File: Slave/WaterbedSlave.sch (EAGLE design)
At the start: 10 parts

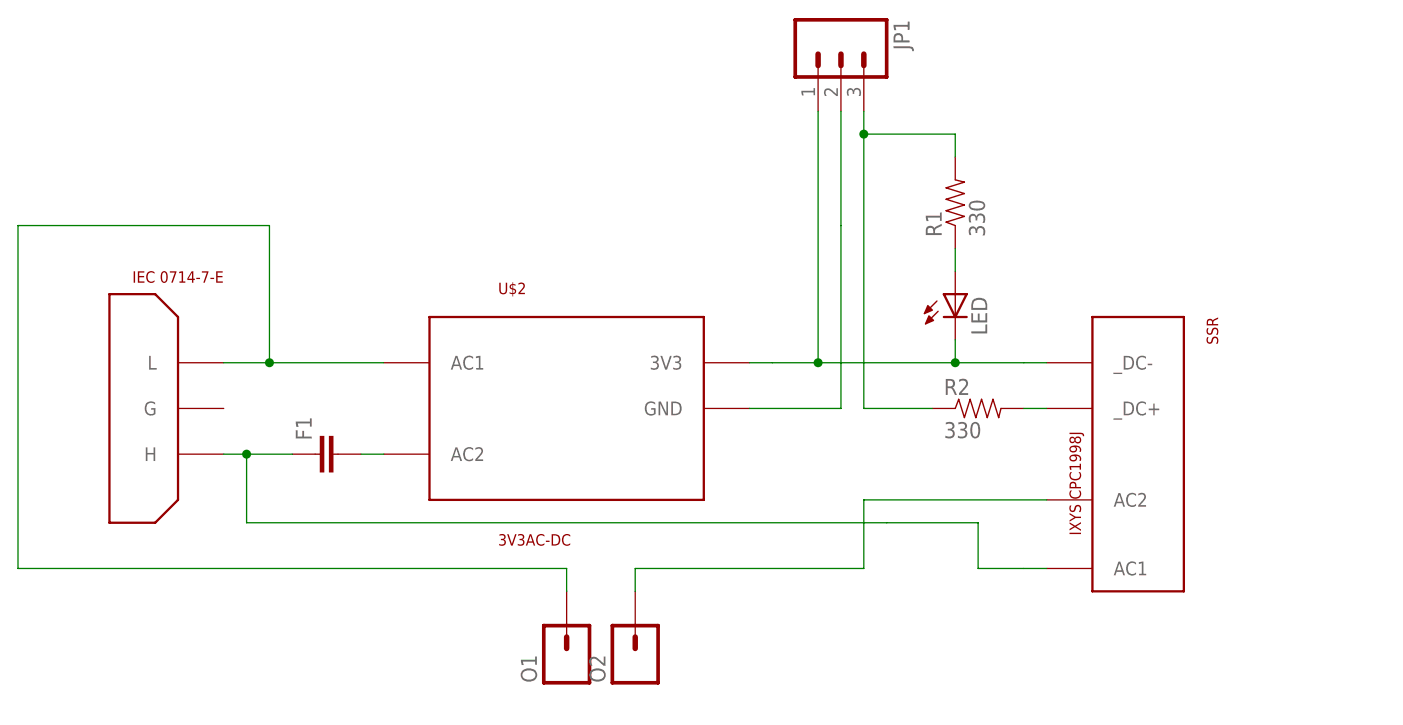
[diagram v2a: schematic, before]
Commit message: The cheap AC-DC sucked. Using trusted brand.
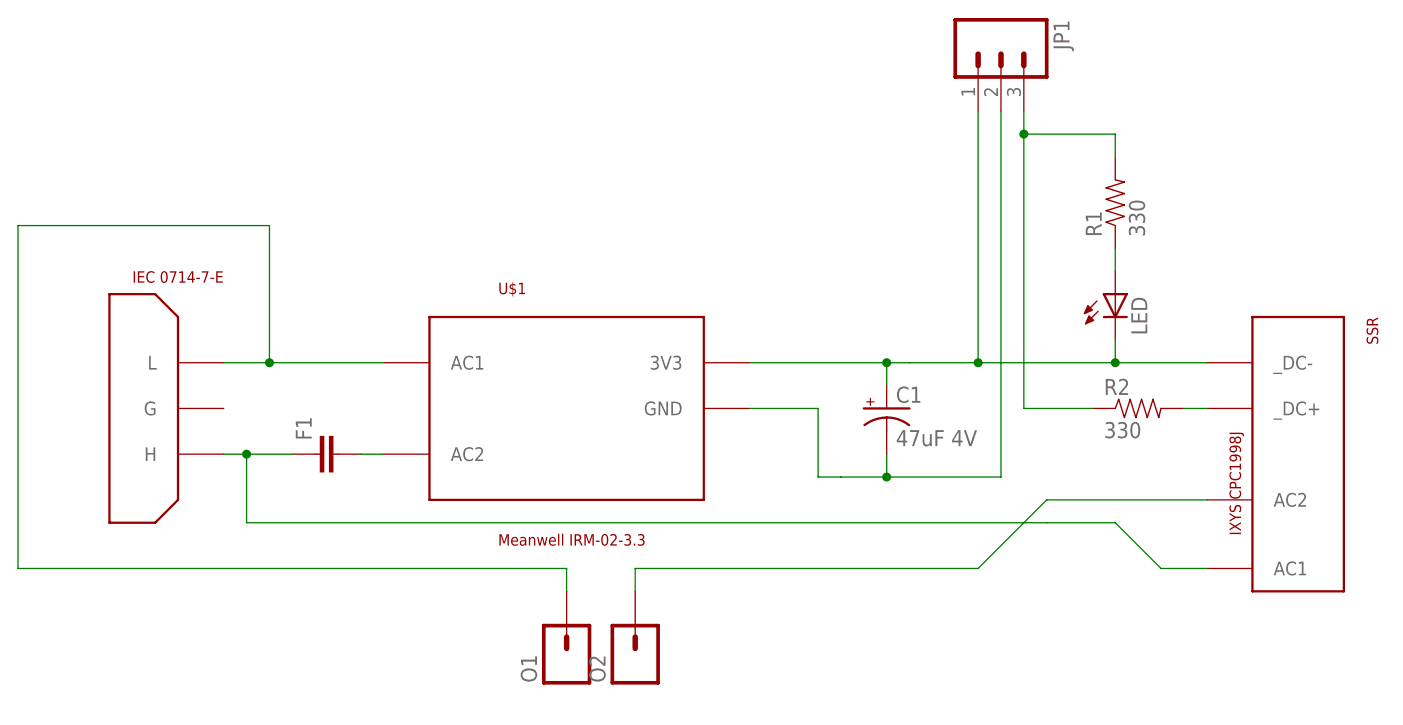
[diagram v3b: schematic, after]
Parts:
- removed U$2: 3V3AC-DC, CuriousTech:RAC02-3.3SCCHEAP
- added C1: 47uF 4V, SparkFun-Capacitors:CAP_POLPTH2
- added U$1: Meanwell IRM-02-3.3, CuriousTech:RAC02-3.3SC
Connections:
- net GND: now also C1.+, U$1.3V3; no longer U$2.3V3
- net N$1: now also U$1.AC1; no longer U$2.AC1
- net N$15: now also C1.-, U$1.GND; no longer U$2.GND
- net N$2: now also U$1.AC2; no longer U$2.AC2
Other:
- moved on the sheet: JP1, LED, R1, R2, SSR
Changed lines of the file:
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@@
 <part name="R1" library="SparkFun-Resistors" deviceset="RESISTOR" device="0805-RES" value="330"/>
 <part name="SSR" library="CuriousTech" deviceset="SSR-5A-240VAC" device="I4-PAC" value="IXYS CPC1998J"/>
-<part name="U$2" library="CuriousTech" deviceset="RAC02-3.3SC" device="CHEAP" value="3V3AC-DC"/>
 <part name="R2" library="SparkFun-Resistors" deviceset="RESISTOR" device="0805-RES" value="330"/>
+<part name="U$1" library="CuriousTech" deviceset="RAC02-3.3SC" device="" value="Meanwell IRM-02-3.3"/>
+<part name="C1" library="SparkFun-Capacitors" deviceset="CAP_POL" device="PTH2" value="47uF 4V"/>
 </parts>
 <sheets>
@@
 </plain>
 <instances>
-<instance part="JP1" gate="G$1" x="91.44" y="101.6" rot="R270"/>
+<instance part="JP1" gate="G$1" x="109.22" y="101.6" rot="R270"/>
 <instance part="U$3" gate="G$1" x="17.78" y="55.88" rot="MR180"/>
 <instance part="O1" gate="G$1" x="60.96" y="33.02" rot="R90"/>
 <instance part="O2" gate="G$1" x="68.58" y="33.02" rot="R90"/>
 <instance part="F1" gate="G$1" x="35.56" y="55.88" rot="R90"/>
-<instance part="LED" gate="G$1" x="104.14" y="73.66"/>
-<instance part="R1" gate="G$1" x="104.14" y="83.82" rot="R90"/>
-<instance part="SSR" gate="G$1" x="124.46" y="55.88" rot="R270"/>
-<instance part="U$2" gate="G$1" x="60.96" y="60.96"/>
-<instance part="R2" gate="G$1" x="106.68" y="60.96"/>
+<instance part="LED" gate="G$1" x="121.92" y="73.66"/>
+<instance part="R1" gate="G$1" x="121.92" y="83.82" rot="R90"/>
+<instance part="SSR" gate="G$1" x="142.24" y="55.88" rot="R270"/>
+<instance part="R2" gate="G$1" x="124.46" y="60.96"/>
+<instance part="U$1" gate="G$1" x="60.96" y="60.96"/>
+<instance part="C1" gate="G$1" x="96.52" y="60.96"/>
 </instances>
 <busses>
@@
 <segment>
 <pinref part="JP1" gate="G$1" pin="1"/>
-<wire x1="88.9" y1="66.04" x2="88.9" y2="93.98" width="0.1524" layer="91"/>
-<junction x="88.9" y="66.04"/>
-<wire x1="104.14" y1="66.04" x2="88.9" y2="66.04" width="0.1524" layer="91"/>
-<wire x1="81.28" y1="66.04" x2="83.82" y2="66.04" width="0.1524" layer="91"/>
-<wire x1="83.82" y1="66.04" x2="88.9" y2="66.04" width="0.1524" layer="91"/>
+<wire x1="106.68" y1="66.04" x2="106.68" y2="93.98" width="0.1524" layer="91"/>
+<junction x="106.68" y="66.04"/>
+<wire x1="121.92" y1="66.04" x2="106.68" y2="66.04" width="0.1524" layer="91"/>
+<wire x1="81.28" y1="66.04" x2="96.52" y2="66.04" width="0.1524" layer="91"/>
 <pinref part="LED" gate="G$1" pin="C"/>
-<wire x1="104.14" y1="68.58" x2="104.14" y2="66.04" width="0.1524" layer="91"/>
-<wire x1="104.14" y1="66.04" x2="111.76" y2="66.04" width="0.1524" layer="91"/>
-<junction x="104.14" y="66.04"/>
-<wire x1="111.76" y1="66.04" x2="114.3" y2="66.04" width="0.1524" layer="91"/>
+<wire x1="96.52" y1="66.04" x2="99.06" y2="66.04" width="0.1524" layer="91"/>
+<wire x1="99.06" y1="66.04" x2="106.68" y2="66.04" width="0.1524" layer="91"/>
+<wire x1="121.92" y1="68.58" x2="121.92" y2="66.04" width="0.1524" layer="91"/>
+<wire x1="121.92" y1="66.04" x2="132.08" y2="66.04" width="0.1524" layer="91"/>
+<junction x="121.92" y="66.04"/>
 <pinref part="SSR" gate="G$1" pin="_DC-"/>
-<pinref part="U$2" gate="G$1" pin="3V3"/>
+<pinref part="U$1" gate="G$1" pin="3V3"/>
+<pinref part="C1" gate="G$1" pin="+"/>
+<wire x1="96.52" y1="63.5" x2="96.52" y2="66.04" width="0.1524" layer="91"/>
+<junction x="96.52" y="66.04"/>
 </segment>
 </net>
 <net name="N$15" class="0">
 <segment>
-<wire x1="81.28" y1="60.96" x2="91.44" y2="60.96" width="0.1524" layer="91"/>
+<wire x1="81.28" y1="60.96" x2="88.9" y2="60.96" width="0.1524" layer="91"/>
 <pinref part="JP1" gate="G$1" pin="2"/>
-<wire x1="91.44" y1="60.96" x2="91.44" y2="81.28" width="0.1524" layer="91"/>
-<wire x1="91.44" y1="81.28" x2="91.44" y2="93.98" width="0.1524" layer="91"/>
-<pinref part="U$2" gate="G$1" pin="GND"/>
+<wire x1="88.9" y1="60.96" x2="88.9" y2="53.34" width="0.1524" layer="91"/>
+<wire x1="88.9" y1="53.34" x2="91.44" y2="53.34" width="0.1524" layer="91"/>
+<wire x1="91.44" y1="53.34" x2="96.52" y2="53.34" width="0.1524" layer="91"/>
+<wire x1="96.52" y1="53.34" x2="109.22" y2="53.34" width="0.1524" layer="91"/>
+<wire x1="109.22" y1="53.34" x2="109.22" y2="93.98" width="0.1524" layer="91"/>
+<pinref part="U$1" gate="G$1" pin="GND"/>
+<pinref part="C1" gate="G$1" pin="-"/>
+<wire x1="96.52" y1="55.88" x2="96.52" y2="53.34" width="0.1524" layer="91"/>
+<junction x="96.52" y="53.34"/>
 </segment>
 </net>
@@
 <segment>
 <pinref part="JP1" gate="G$1" pin="3"/>
-<wire x1="93.98" y1="93.98" x2="93.98" y2="91.44" width="0.1524" layer="91"/>
-<wire x1="93.98" y1="91.44" x2="93.98" y2="60.96" width="0.1524" layer="91"/>
+<wire x1="111.76" y1="93.98" x2="111.76" y2="91.44" width="0.1524" layer="91"/>
+<wire x1="111.76" y1="91.44" x2="111.76" y2="60.96" width="0.1524" layer="91"/>
 <pinref part="R1" gate="G$1" pin="2"/>
-<wire x1="104.14" y1="88.9" x2="104.14" y2="91.44" width="0.1524" layer="91"/>
-<wire x1="104.14" y1="91.44" x2="93.98" y2="91.44" width="0.1524" layer="91"/>
-<junction x="93.98" y="91.44"/>
+<wire x1="121.92" y1="88.9" x2="121.92" y2="91.44" width="0.1524" layer="91"/>
+<wire x1="121.92" y1="91.44" x2="111.76" y2="91.44" width="0.1524" layer="91"/>
+<junction x="111.76" y="91.44"/>
 <pinref part="R2" gate="G$1" pin="1"/>
-<wire x1="93.98" y1="60.96" x2="101.6" y2="60.96" width="0.1524" layer="91"/>
+<wire x1="111.76" y1="60.96" x2="119.38" y2="60.96" width="0.1524" layer="91"/>
 </segment>
 </net>
@@
 <wire x1="27.94" y1="81.28" x2="27.94" y2="66.04" width="0.1524" layer="91"/>
 <pinref part="O1" gate="G$1" pin="1"/>
-<pinref part="U$2" gate="G$1" pin="AC1"/>
 <wire x1="27.94" y1="66.04" x2="40.64" y2="66.04" width="0.1524" layer="91"/>
 <junction x="27.94" y="66.04"/>
+<pinref part="U$1" gate="G$1" pin="AC1"/>
 </segment>
 </net>
@@
 <pinref part="R1" gate="G$1" pin="1"/>
 <pinref part="LED" gate="G$1" pin="A"/>
-<wire x1="104.14" y1="78.74" x2="104.14" y2="76.2" width="0.1524" layer="91"/>
+<wire x1="121.92" y1="78.74" x2="121.92" y2="76.2" width="0.1524" layer="91"/>
 </segment>
 </net>
@@
 <segment>
 <pinref part="F1" gate="G$1" pin="2"/>
-<pinref part="U$2" gate="G$1" pin="AC2"/>
 <wire x1="38.1" y1="55.88" x2="40.64" y2="55.88" width="0.1524" layer="91"/>
+<pinref part="U$1" gate="G$1" pin="AC2"/>
 </segment>
 </net>
@@
 <wire x1="68.58" y1="43.18" x2="68.58" y2="40.64" width="0.1524" layer="91"/>
 <pinref part="O2" gate="G$1" pin="1"/>
-<wire x1="68.58" y1="43.18" x2="93.98" y2="43.18" width="0.1524" layer="91"/>
-<wire x1="93.98" y1="43.18" x2="93.98" y2="50.8" width="0.1524" layer="91"/>
+<wire x1="68.58" y1="43.18" x2="106.68" y2="43.18" width="0.1524" layer="91"/>
+<wire x1="106.68" y1="43.18" x2="114.3" y2="50.8" width="0.1524" layer="91"/>
 <pinref part="SSR" gate="G$1" pin="AC2"/>
-<wire x1="93.98" y1="50.8" x2="114.3" y2="50.8" width="0.1524" layer="91"/>
+<wire x1="114.3" y1="50.8" x2="132.08" y2="50.8" width="0.1524" layer="91"/>
 </segment>
 </net>
@@
 <segment>
 <wire x1="25.4" y1="55.88" x2="25.4" y2="48.26" width="0.1524" layer="91"/>
-<wire x1="25.4" y1="48.26" x2="96.52" y2="48.26" width="0.1524" layer="91"/>
+<wire x1="25.4" y1="48.26" x2="114.3" y2="48.26" width="0.1524" layer="91"/>
 <pinref part="U$3" gate="G$1" pin="H"/>
 <wire x1="22.86" y1="55.88" x2="25.4" y2="55.88" width="0.1524" layer="91"/>
@@
 <wire x1="25.4" y1="55.88" x2="30.48" y2="55.88" width="0.1524" layer="91"/>
 <junction x="25.4" y="55.88"/>
-<wire x1="96.52" y1="48.26" x2="106.68" y2="48.26" width="0.1524" layer="91"/>
-<wire x1="106.68" y1="48.26" x2="106.68" y2="43.18" width="0.1524" layer="91"/>
-<wire x1="111.76" y1="43.18" x2="114.3" y2="43.18" width="0.1524" layer="91"/>
+<wire x1="114.3" y1="48.26" x2="121.92" y2="48.26" width="0.1524" layer="91"/>
+<wire x1="121.92" y1="48.26" x2="127" y2="43.18" width="0.1524" layer="91"/>
+<wire x1="129.54" y1="43.18" x2="132.08" y2="43.18" width="0.1524" layer="91"/>
 <pinref part="SSR" gate="G$1" pin="AC1"/>
-<wire x1="106.68" y1="43.18" x2="111.76" y2="43.18" width="0.1524" layer="91"/>
+<wire x1="127" y1="43.18" x2="129.54" y2="43.18" width="0.1524" layer="91"/>
 </segment>
 </net>
@@
 <segment>
 <pinref part="SSR" gate="G$1" pin="_DC+"/>
-<wire x1="111.76" y1="60.96" x2="114.3" y2="60.96" width="0.1524" layer="91"/>
+<wire x1="129.54" y1="60.96" x2="132.08" y2="60.96" width="0.1524" layer="91"/>
 <pinref part="R2" gate="G$1" pin="2"/>
 </segment>
